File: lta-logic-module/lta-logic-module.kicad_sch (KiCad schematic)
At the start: 24 parts

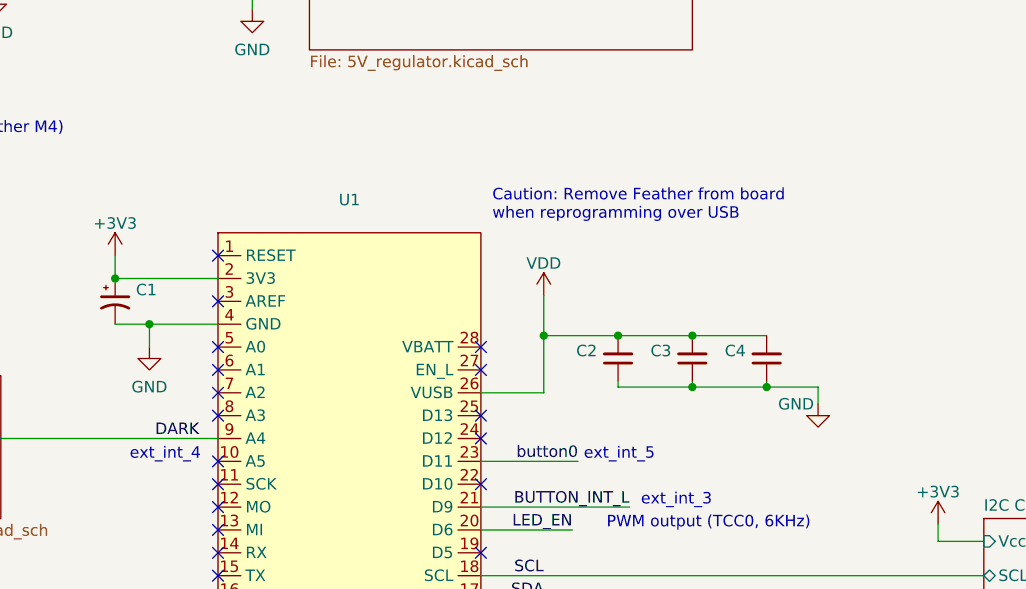
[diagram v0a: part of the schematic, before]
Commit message: Add indicator LED to SW1 enabled.
Adds 220K pull-down resistor to DARK signal. (Validated.)
Update solder thief pads and process direction indicator.
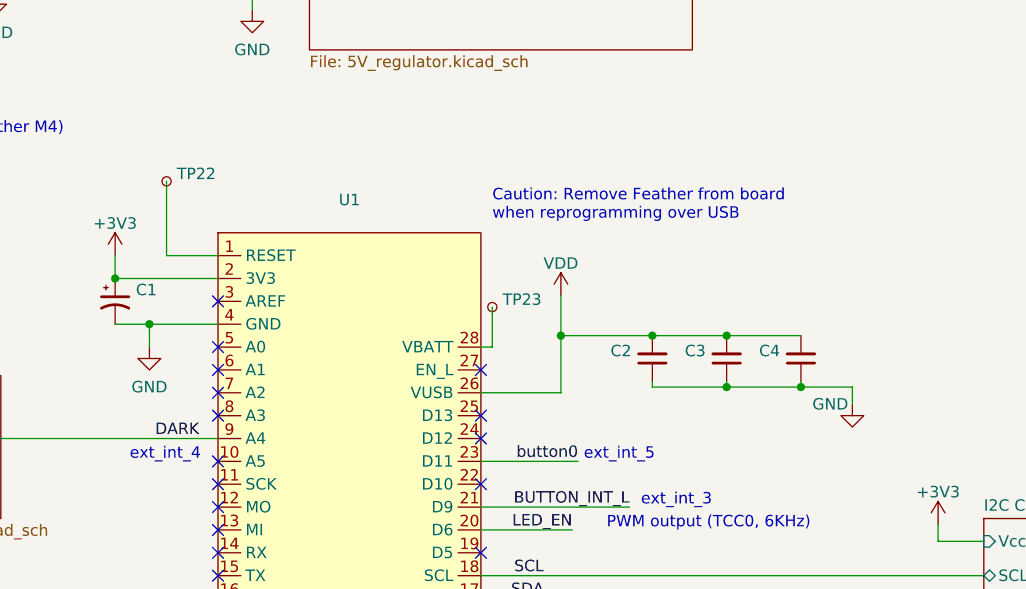
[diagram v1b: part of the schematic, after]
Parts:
- added TP22, TP23: (no value), symbol Connector:TestPoint_Small
- J1: Comment Molex Micro-Fit 3 2-pin -> Molex Micro-Fit3, 2-pin
- U1: Comment Use 1x16 and 1x12 female THT headers 2.54mm pitch, 6.5--8.0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 -> Use 1x16 and 1x12 female THT headers, gold mating, 2.54mm p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
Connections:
- net at U1.1 (RESET): now also TP22.1
- net at U1.28 (VBATT): now also TP23.1
- no-connect marks 21 -> 19
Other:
- moved on the sheet: C2, C3, C4

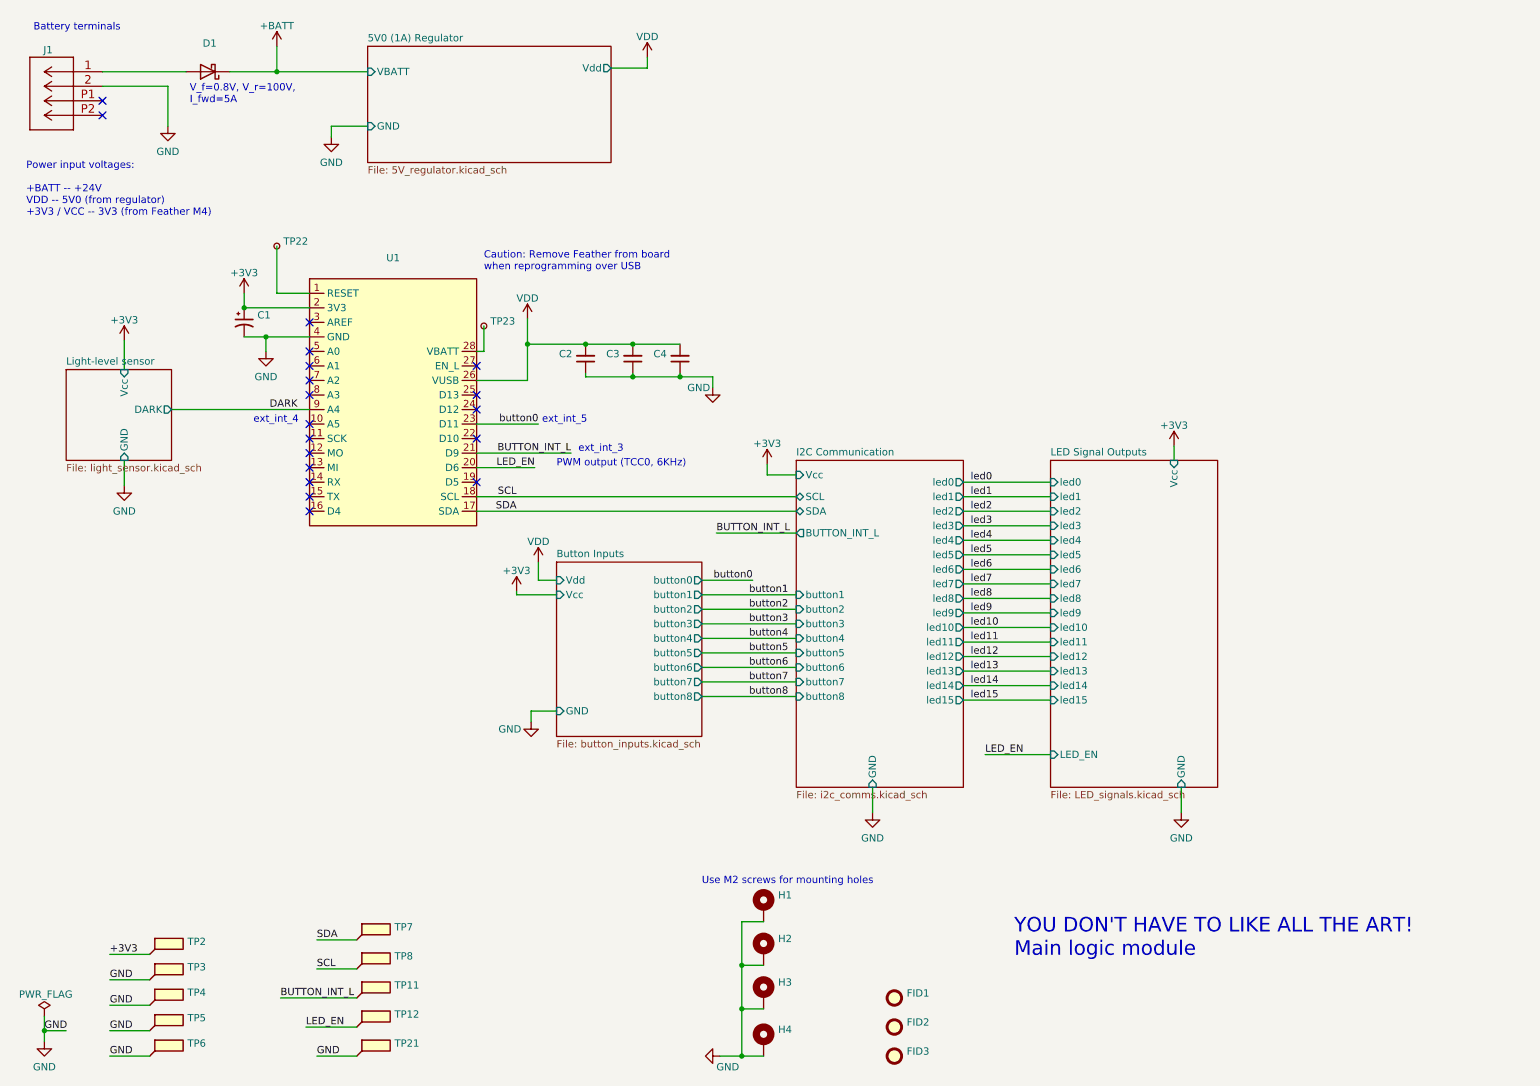
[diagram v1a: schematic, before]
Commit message: Generate logic module 2022-05-08 v1.0 fab documentation.
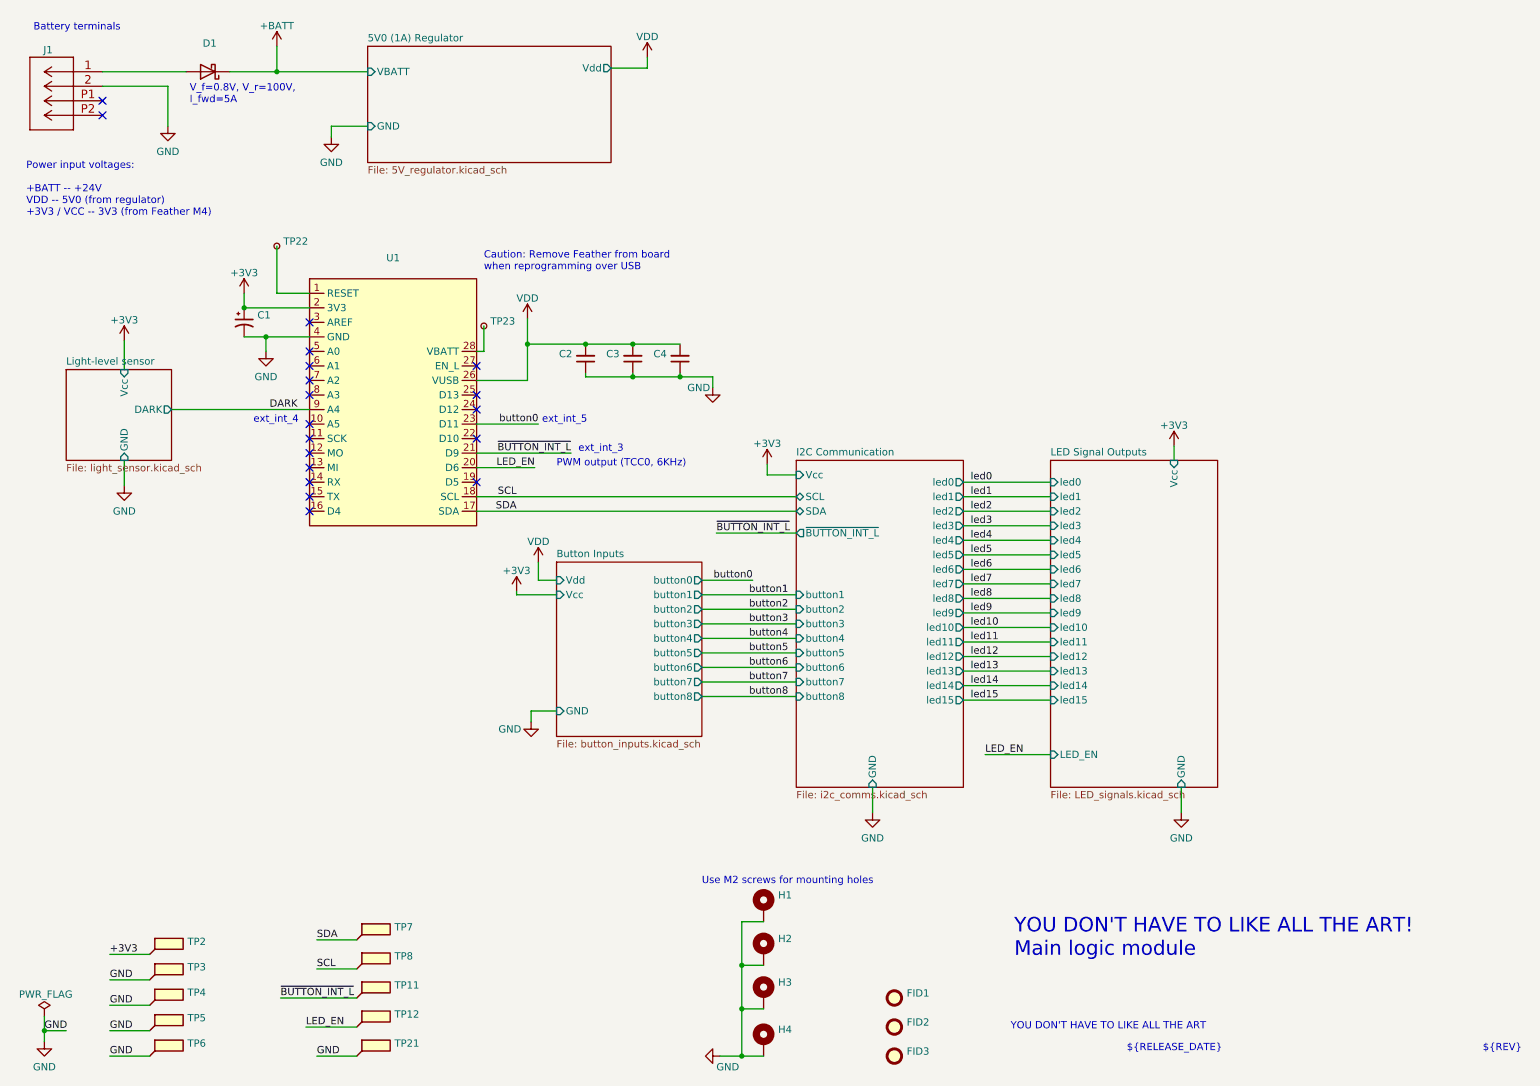
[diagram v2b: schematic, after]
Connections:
- net BUTTON_INT_L renamed ~{BUTTON_INT_L}
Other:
- sheet I2C Communication ports: added ~{BUTTON_INT_L}; removed BUTTON_INT_L
- note added: "${RELEASE_DATE}"
- note added: "${REV}"
- note added: "YOU DON'T HAVE TO LIKE ALL THE ART"
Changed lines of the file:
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@@
     (effects (font (size 2.54 2.54)) (justify left bottom))
+  )
+  (text "${REV}" (at 269.24 194.31 0)
+    (effects (font (size 1.27 1.27)) (justify left bottom))
   )
   (text "ext_int_4" (at 62.23 84.455 180)
@@
     (effects (font (size 1.27 1.27)) (justify left bottom))
   )
+  (text "YOU DON'T HAVE TO LIKE ALL THE ART" (at 186.69 190.5 0)
+    (effects (font (size 1.27 1.27)) (justify left bottom))
+  )
+  (text "${RELEASE_DATE}" (at 207.01 194.31 0)
+    (effects (font (size 1.27 1.27)) (justify left bottom))
+  )
   (text "Use M2 screws for mounting holes " (at 132.715 165.1 0)
     (effects (font (size 1.27 1.27)) (justify left bottom))
@@
     (effects (font (size 1.27 1.27)) (justify left bottom))
   )
-  (label "BUTTON_INT_L" (at 109.855 89.535 180)
+  (label "~{BUTTON_INT_L}" (at 109.855 89.535 180)
     (effects (font (size 1.27 1.27)) (justify right bottom))
   )
@@
     (effects (font (size 1.27 1.27)) (justify right bottom))
   )
-  (label "BUTTON_INT_L" (at 59.055 184.785 0)
+  (label "~{BUTTON_INT_L}" (at 59.055 184.785 0)
     (effects (font (size 1.27 1.27)) (justify left bottom))
   )
@@
     (effects (font (size 1.27 1.27)) (justify left bottom))
   )
-  (label "BUTTON_INT_L" (at 135.255 103.505 0)
+  (label "~{BUTTON_INT_L}" (at 135.255 103.505 0)
     (effects (font (size 1.27 1.27)) (justify left bottom))
   )
@@
       (effects (font (size 1.27 1.27)) (justify left))
     )
-    (pin "BUTTON_INT_L" output (at 149.225 103.505 180)
-      (effects (font (size 1.27 1.27)) (justify left))
-    )
+    (pin "~{BUTTON_INT_L}" output (at 149.225 103.505 180)
+      (effects (font (size 1.27 1.27)) (justify left))
+    )

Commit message: Update logic module power budget from button LED measurements.
Button LEDs draw ~11mA each (98 mA total) empirically; not the ~20mA each
I initially guessed for estimating purposes.
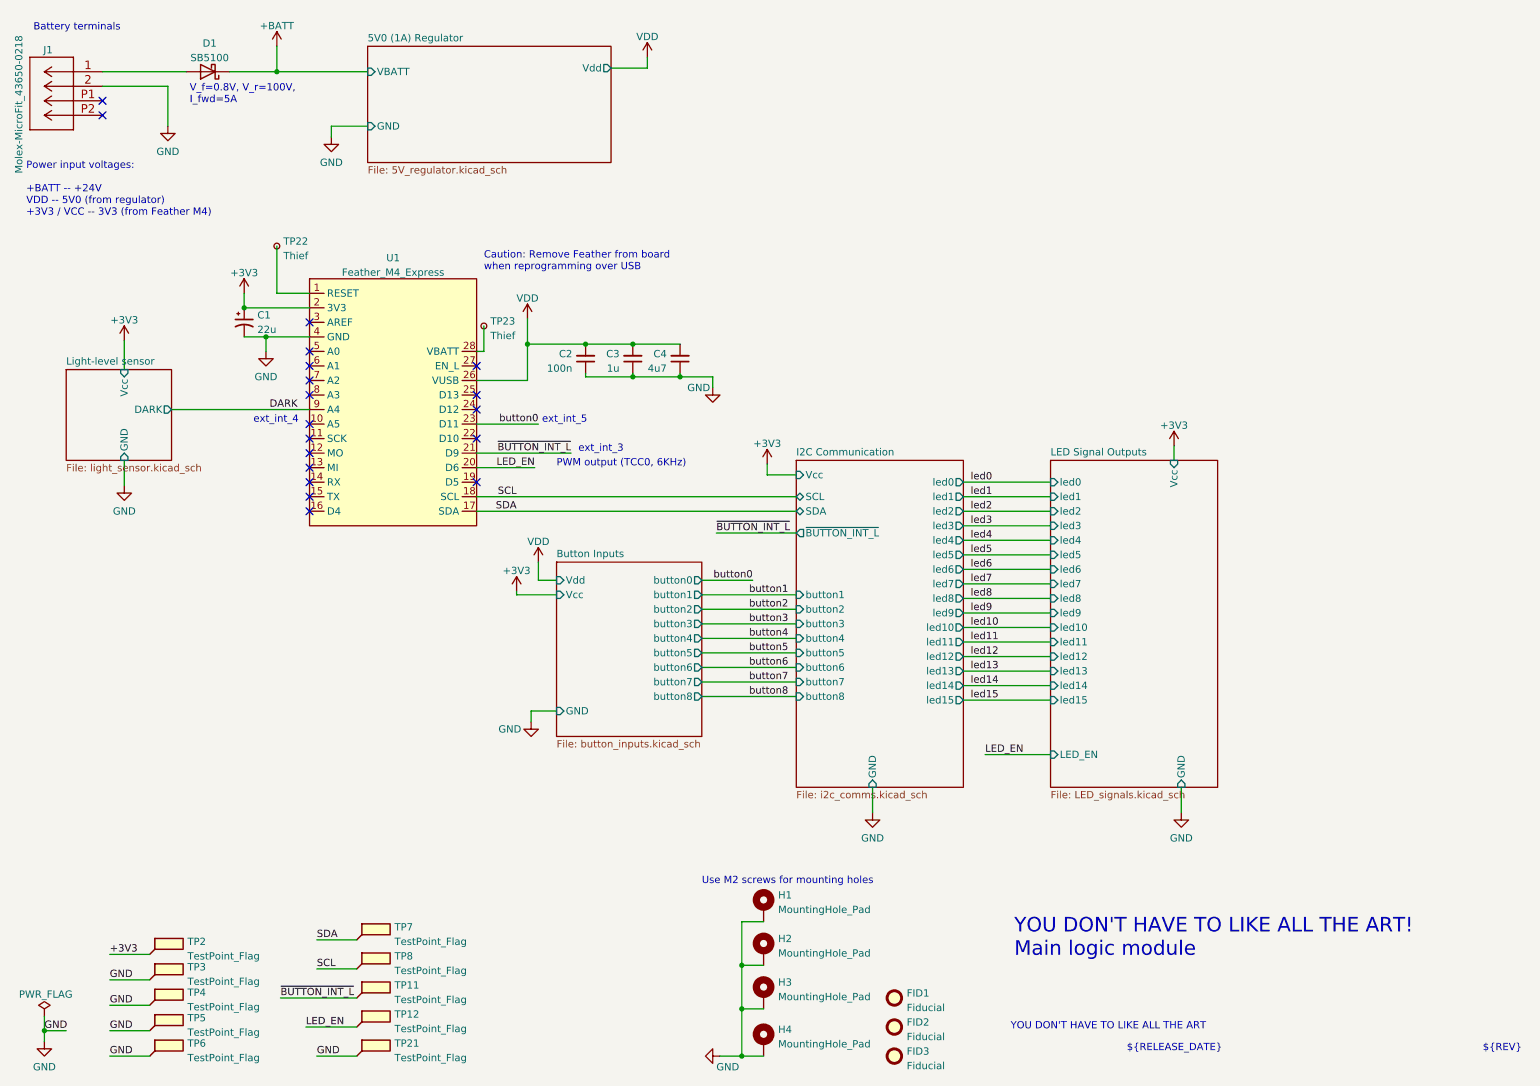
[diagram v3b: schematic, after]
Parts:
- C1: value (none) -> 22u; footprint (none) -> Capacitor_Tantalum_SMD:CP_EIA-7343-30_AVX-N
- C2: value (none) -> 100n; footprint (none) -> Capacitor_SMD:C_0603_1608Metric
- C3: value (none) -> 1u; footprint (none) -> Capacitor_SMD:C_0603_1608Metric
- C4: value (none) -> 4u7; footprint (none) -> Capacitor_SMD:C_0805_2012Metric
- D1: value (none) -> SB5100; footprint (none) -> Diode_THT:D_DO-201AD_P15.24mm_Horizontal
- FID1, FID2, FID3: value (none) -> Fiducial; footprint (none) -> Fiducial:Fiducial_1mm_Mask2mm
- H1, H2, H3, H4: value (none) -> MountingHole_Pad; footprint (none) -> MountingHole:MountingHole_2.2mm_M2_ISO7380_Pad
- J1: value (none) -> Molex-MicroFit_43650-0218; footprint (none) -> Aaron_THT:Molex-Microfit-43650-0218
- TP11, TP12, TP2, TP21, TP3, TP4, TP5, TP6, TP7, TP8: value (none) -> TestPoint_Flag; footprint (none) -> Aaron_THT:TestPoint_THTPad_1.0x1.0mm_Drill0.3mm
- TP22, TP23: value (none) -> Thief; footprint (none) -> Aaron_Pads:Pad_1.5x1.5mm
- U1: value (none) -> Feather_M4_Express; footprint (none) -> aaron-imported-parts:Arduino_Feather_M4_Express_PinHeaders
